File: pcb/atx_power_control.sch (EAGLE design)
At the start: 61 parts, among them IC2 REG1117, IC3 STM32F042F4, IC4 MY_7905DT, J1 ATX24RH, SW1 324_SW, SW2 324_SW, SW3 324_SW, SW4 324_SW, SW5 324_SW, SW7 324_SW, U1 USBC_16P, U2 USBC_16P

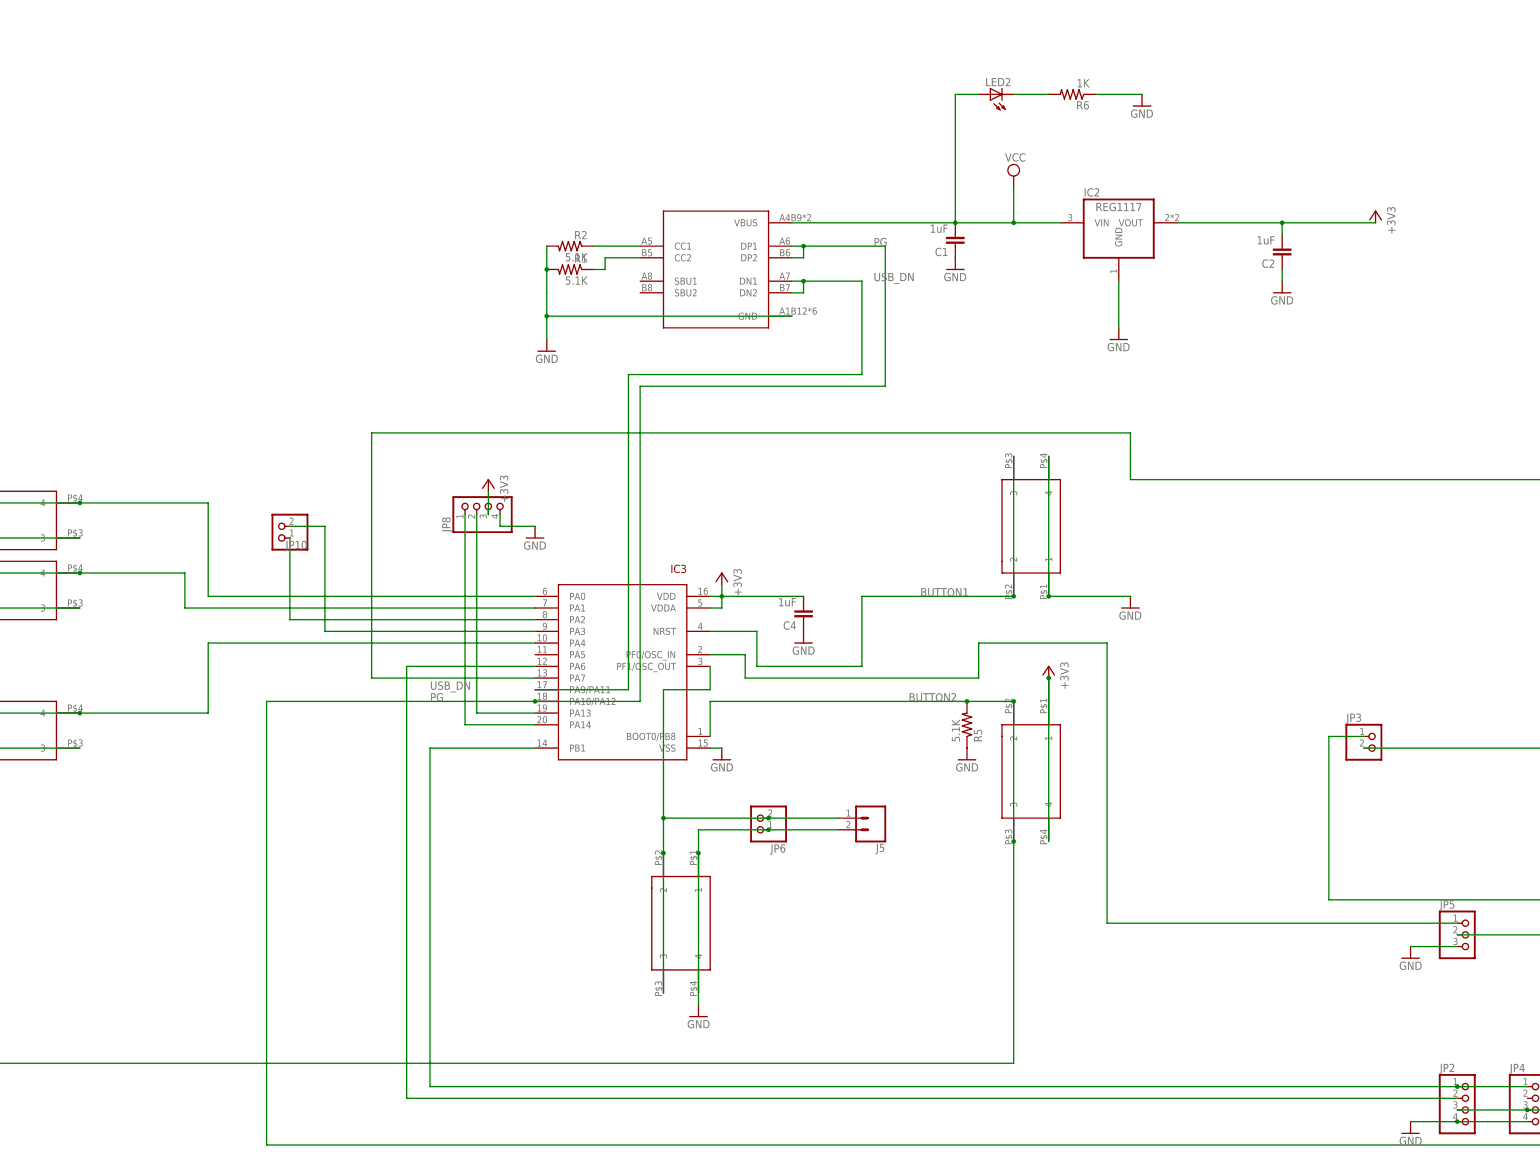
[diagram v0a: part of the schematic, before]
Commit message: added ds18b20 header
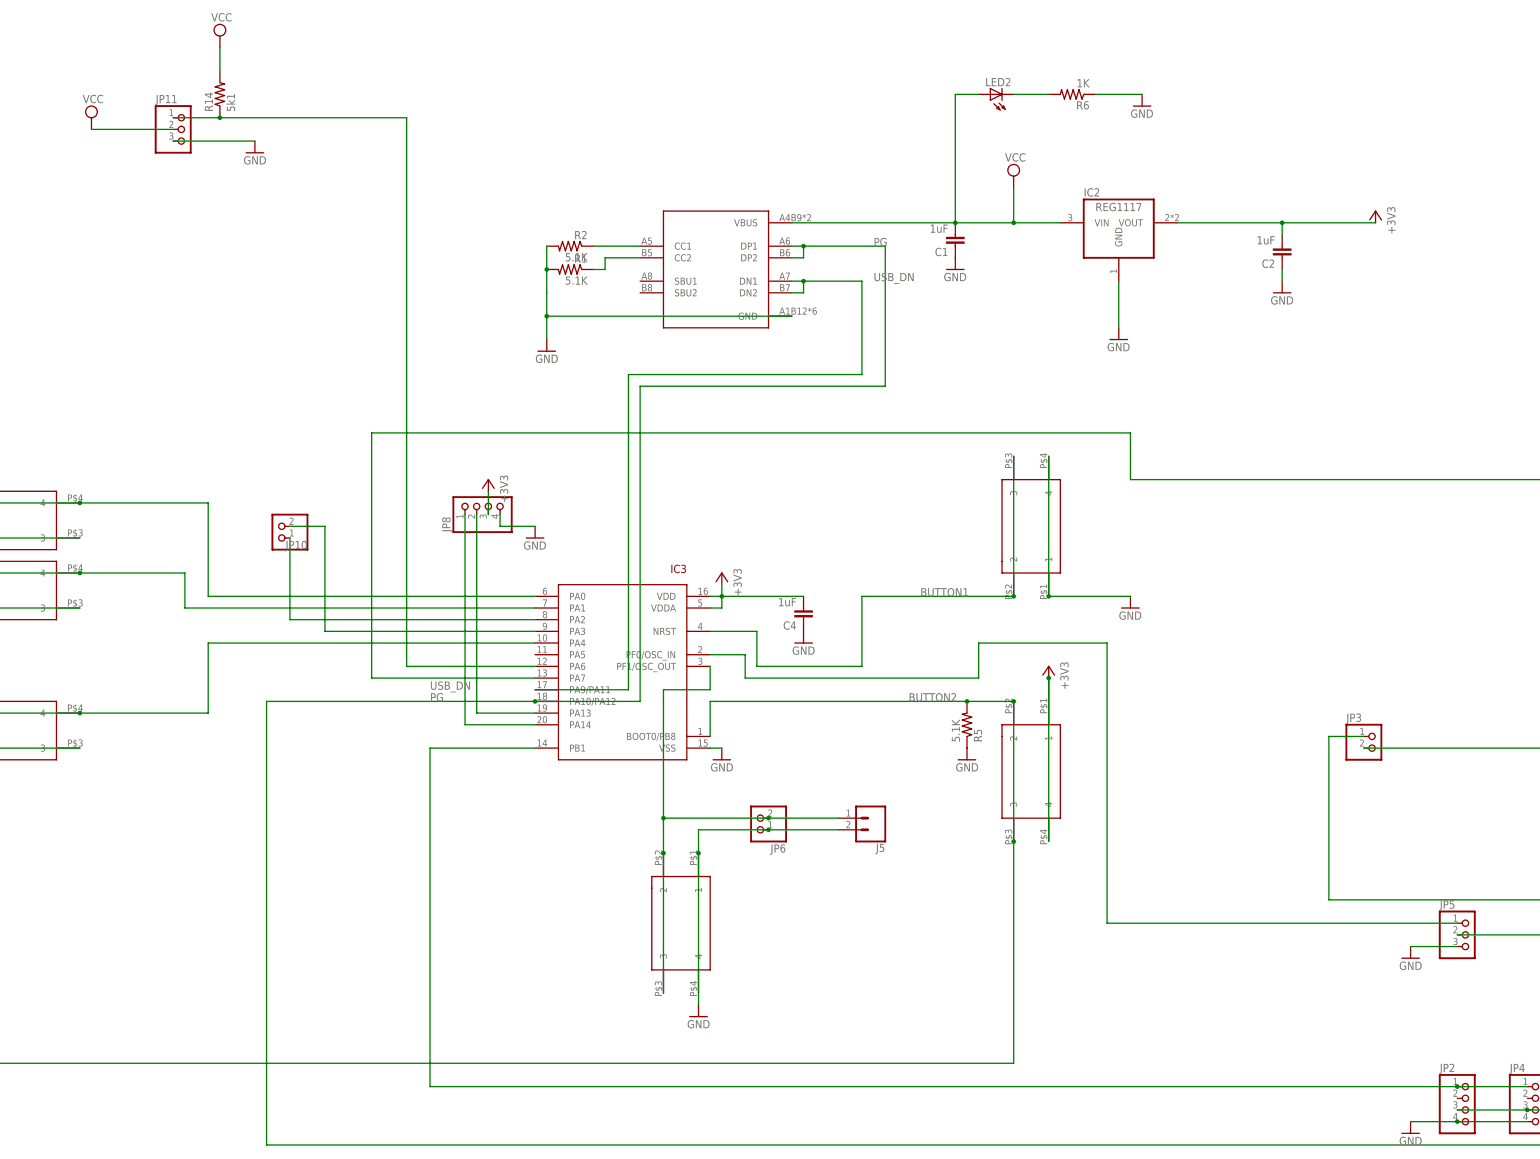
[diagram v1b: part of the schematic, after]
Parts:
- added JP11: (no value), adafruit_changed:PINHD-1X3CB
- added R14: 5k1, SparkFun-Passives:RESISTOR0805-RES
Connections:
- net GND: now also JP11.3
- net N$6: now also JP11.1, R14.1; no longer JP2.2
- net VCC: now also JP11.2, R14.2
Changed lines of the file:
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@@
 <part name="JP4" library="pinhead" library_urn="urn:adsk.eagle:library:325" deviceset="PINHD-1X4" device="" package3d_urn="urn:adsk.eagle:package:22407/2"/>
 <part name="JP12" library="adafruit_changed" deviceset="PINHD-1X6" device=""/>
+<part name="R14" library="SparkFun-Passives" deviceset="RESISTOR" device="0805-RES" value="5k1"/>
+<part name="JP11" library="adafruit_changed" deviceset="PINHD-1X3" device="CB"/>
+<part name="SUPPLY1" library="supply2" library_urn="urn:adsk.eagle:library:372" deviceset="VCC" device=""/>
+<part name="GND34" library="supply1" deviceset="GND" device=""/>
+<part name="SUPPLY2" library="supply2" library_urn="urn:adsk.eagle:library:372" deviceset="VCC" device=""/>
 </parts>
 <sheets>
@@
 <attribute name="NAME" x="273.05" y="71.755" size="1.778" layer="95"/>
 <attribute name="VALUE" x="273.05" y="50.8" size="1.778" layer="96"/>
+</instance>
+<instance part="R14" gate="G$1" x="-86.36" y="149.86" smashed="yes" rot="R90">
+<attribute name="NAME" x="-87.8586" y="146.05" size="1.778" layer="95" rot="R90"/>
+<attribute name="VALUE" x="-83.058" y="146.05" size="1.778" layer="96" rot="R90"/>
+</instance>
+<instance part="JP11" gate="A" x="-93.98" y="142.24" smashed="yes">
+<attribute name="NAME" x="-100.33" y="147.955" size="1.778" layer="95"/>
+<attribute name="VALUE" x="-100.33" y="134.62" size="1.778" layer="96"/>
+</instance>
+<instance part="SUPPLY1" gate="G$1" x="-114.3" y="144.78" smashed="yes">
+<attribute name="VALUE" x="-116.205" y="147.955" size="1.778" layer="96"/>
+</instance>
+<instance part="GND34" gate="1" x="-78.74" y="137.16" smashed="yes" rot="MR0">
+<attribute name="VALUE" x="-76.2" y="134.62" size="1.778" layer="96" rot="MR0"/>
+</instance>
+<instance part="SUPPLY2" gate="G$1" x="-86.36" y="162.56" smashed="yes">
+<attribute name="VALUE" x="-88.265" y="165.735" size="1.778" layer="96"/>
 </instance>
 </instances>
@@
 <junction x="317.5" y="76.2"/>
 </segment>
+<segment>
+<pinref part="GND34" gate="1" pin="GND"/>
+<pinref part="JP11" gate="A" pin="3"/>
+<wire x1="-78.74" y1="139.7" x2="-96.52" y2="139.7" width="0.1524" layer="91"/>
+</segment>
 </net>
 <net name="+3V3" class="0">
@@
 <wire x1="208.28" y1="7.62" x2="205.74" y2="7.62" width="0.1524" layer="91"/>
 <wire x1="205.74" y1="7.62" x2="162.56" y2="7.62" width="0.1524" layer="91"/>
+</segment>
+<segment>
+<pinref part="JP11" gate="A" pin="2"/>
+<pinref part="SUPPLY1" gate="G$1" pin="VCC"/>
+<wire x1="-96.52" y1="142.24" x2="-114.3" y2="142.24" width="0.1524" layer="91"/>
+</segment>
+<segment>
+<pinref part="R14" gate="G$1" pin="2"/>
+<pinref part="SUPPLY2" gate="G$1" pin="VCC"/>
+<wire x1="-86.36" y1="160.02" x2="-86.36" y2="154.94" width="0.1524" layer="91"/>
 </segment>
 </net>
@@
 <net name="N$6" class="0">
 <segment>
-<pinref part="JP2" gate="A" pin="2"/>
-<wire x1="182.88" y1="-68.58" x2="-45.72" y2="-68.58" width="0.1524" layer="91"/>
-<wire x1="-45.72" y1="-68.58" x2="-45.72" y2="25.4" width="0.1524" layer="91"/>
 <pinref part="IC3" gate="G$1" pin="PA6"/>
 <wire x1="-45.72" y1="25.4" x2="-17.78" y2="25.4" width="0.1524" layer="91"/>
-</segment>
-</net>
+<pinref part="JP11" gate="A" pin="1"/>
+<wire x1="-45.72" y1="25.4" x2="-45.72" y2="144.78" width="0.1524" layer="91"/>
+<wire x1="-45.72" y1="144.78" x2="-86.36" y2="144.78" width="0.1524" layer="91"/>
+<pinref part="R14" gate="G$1" pin="1"/>
+<wire x1="-86.36" y1="144.78" x2="-96.52" y2="144.78" width="0.1524" layer="91"/>
+<junction x="-86.36" y="144.78"/>
+</segment>
+</net>

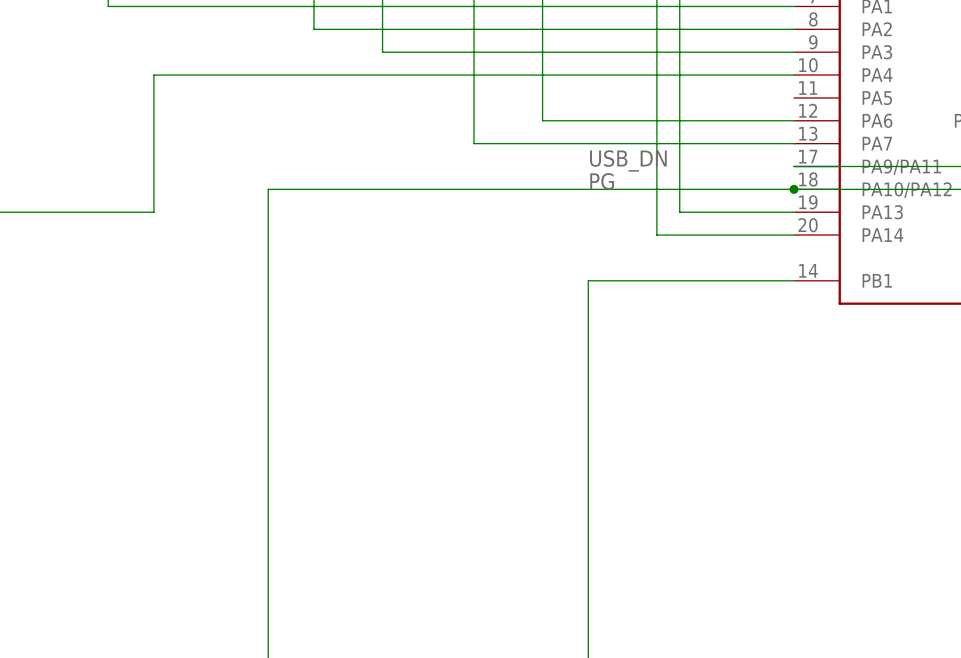
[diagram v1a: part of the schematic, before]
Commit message: added indicator LED
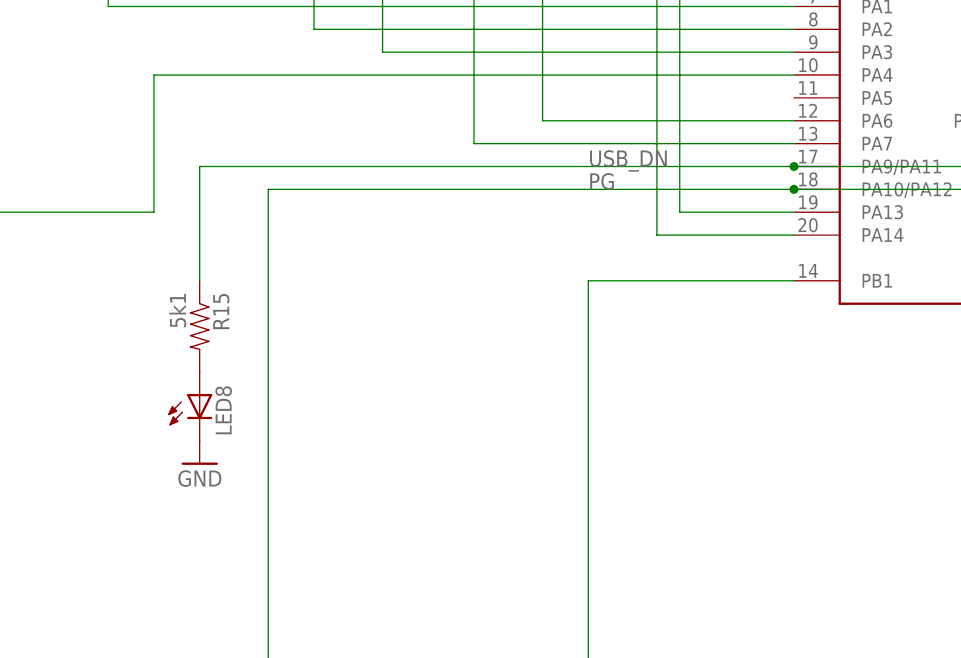
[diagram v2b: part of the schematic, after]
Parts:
- added LED8: (no value), adafruit:LEDCHIP-LED0805
- added R15: 5k1, SparkFun-Passives:RESISTOR0805-RES
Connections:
- new net N$19: LED8.A, R15.2
- net GND: now also LED8.C
- net USB_DN: now also R15.1
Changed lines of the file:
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@@
 <part name="GND34" library="supply1" deviceset="GND" device=""/>
 <part name="SUPPLY2" library="supply2" library_urn="urn:adsk.eagle:library:372" deviceset="VCC" device=""/>
+<part name="R15" library="SparkFun-Passives" deviceset="RESISTOR" device="0805-RES" value="5k1"/>
+<part name="LED8" library="adafruit" deviceset="LED" device="CHIP-LED0805"/>
+<part name="GND36" library="supply1" deviceset="GND" device=""/>
 </parts>
 <sheets>
@@
 <instance part="SUPPLY2" gate="G$1" x="-86.36" y="162.56" smashed="yes">
 <attribute name="VALUE" x="-88.265" y="165.735" size="1.778" layer="96"/>
+</instance>
+<instance part="R15" gate="G$1" x="-83.82" y="2.54" smashed="yes" rot="R270">
+<attribute name="NAME" x="-82.3214" y="6.35" size="1.778" layer="95" rot="R270"/>
+<attribute name="VALUE" x="-87.122" y="6.35" size="1.778" layer="96" rot="R270"/>
+</instance>
+<instance part="LED8" gate="G$1" x="-83.82" y="-5.08" smashed="yes">
+<attribute name="NAME" x="-80.264" y="-9.652" size="1.778" layer="95" rot="R90"/>
+<attribute name="VALUE" x="-78.105" y="-9.652" size="1.778" layer="96" rot="R90"/>
+</instance>
+<instance part="GND36" gate="1" x="-83.82" y="-12.7" smashed="yes" rot="MR0">
+<attribute name="VALUE" x="-81.28" y="-15.24" size="1.778" layer="96" rot="MR0"/>
 </instance>
 </instances>
@@
 <wire x1="-78.74" y1="139.7" x2="-96.52" y2="139.7" width="0.1524" layer="91"/>
 </segment>
+<segment>
+<pinref part="LED8" gate="G$1" pin="C"/>
+<pinref part="GND36" gate="1" pin="GND"/>
+</segment>
 </net>
 <net name="+3V3" class="0">
@@
 <wire x1="2.54" y1="88.9" x2="53.34" y2="88.9" width="0.1524" layer="91"/>
 <wire x1="53.34" y1="88.9" x2="53.34" y2="109.22" width="0.1524" layer="91"/>
+<pinref part="R15" gate="G$1" pin="1"/>
+<wire x1="-17.78" y1="20.32" x2="-83.82" y2="20.32" width="0.1524" layer="91"/>
+<wire x1="-83.82" y1="20.32" x2="-83.82" y2="7.62" width="0.1524" layer="91"/>
+<junction x="-17.78" y="20.32"/>
 </segment>
 </net>
@@
 </segment>
 </net>
+<net name="N$19" class="0">
+<segment>
+<pinref part="R15" gate="G$1" pin="2"/>
+<pinref part="LED8" gate="G$1" pin="A"/>
+</segment>
+</net>

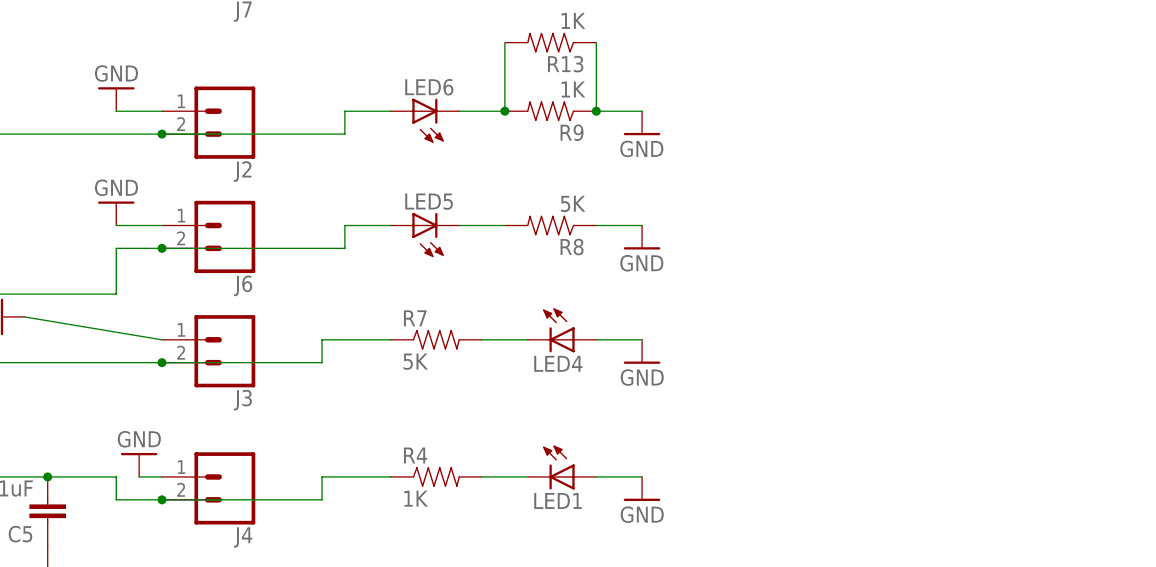
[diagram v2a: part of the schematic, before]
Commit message: adjusted LED resistor value, optimised GND plane
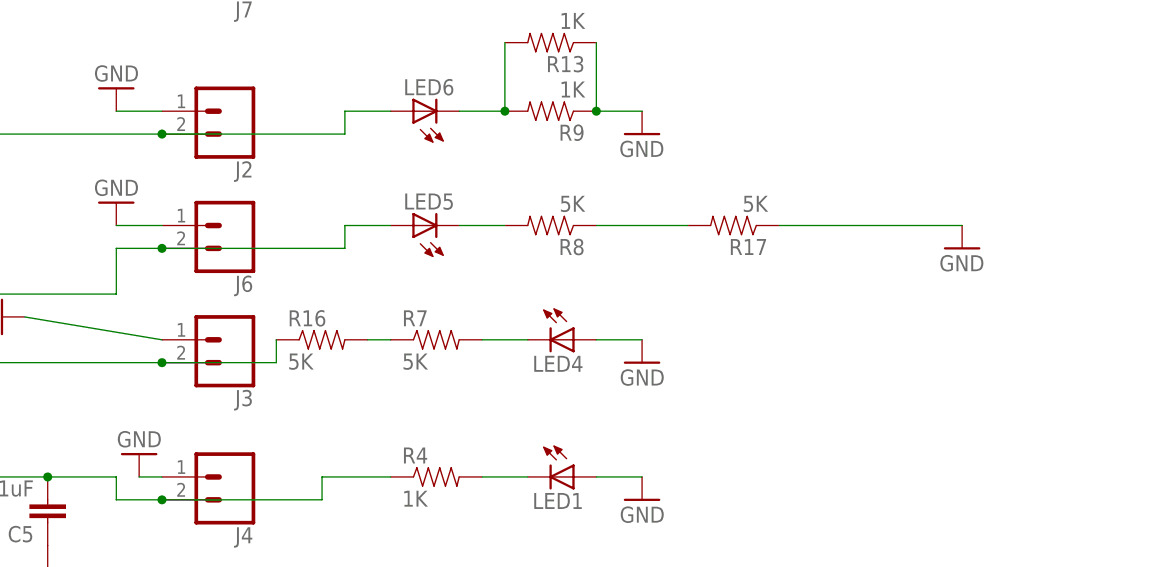
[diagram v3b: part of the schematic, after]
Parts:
- added R16, R17: 5K, SparkFun-Passives:RESISTOR0805-RES
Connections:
- new net N$28: R16.2, R7.1
- new net N$32: R17.2, R8.1
- net GND: now also R17.1; no longer R8.1
- net N$2: now also R16.1; no longer R7.1
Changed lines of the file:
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@@
 <part name="LED8" library="adafruit" deviceset="LED" device="CHIP-LED0805"/>
 <part name="GND36" library="supply1" deviceset="GND" device=""/>
+<part name="R16" library="SparkFun-Passives" deviceset="RESISTOR" device="0805-RES" value="5K"/>
+<part name="R17" library="SparkFun-Passives" deviceset="RESISTOR" device="0805-RES" value="5K"/>
 </parts>
 <sheets>
@@
 <attribute name="VALUE" x="394.97" y="16.002" size="1.778" layer="96" rot="R180"/>
 </instance>
-<instance part="GND19" gate="1" x="401.32" y="10.16" smashed="yes">
-<attribute name="VALUE" x="398.78" y="7.62" size="1.778" layer="96"/>
+<instance part="GND19" gate="1" x="436.88" y="10.16" smashed="yes">
+<attribute name="VALUE" x="434.34" y="7.62" size="1.778" layer="96"/>
 </instance>
 <instance part="LED6" gate="G$1" x="375.92" y="25.4" smashed="yes" rot="R90">
@@
 <instance part="GND36" gate="1" x="-83.82" y="-12.7" smashed="yes" rot="MR0">
 <attribute name="VALUE" x="-81.28" y="-15.24" size="1.778" layer="96" rot="MR0"/>
+</instance>
+<instance part="R16" gate="G$1" x="365.76" y="0" smashed="yes">
+<attribute name="NAME" x="361.95" y="1.4986" size="1.778" layer="95"/>
+<attribute name="VALUE" x="361.95" y="-3.302" size="1.778" layer="96"/>
+</instance>
+<instance part="R17" gate="G$1" x="411.48" y="12.7" smashed="yes" rot="R180">
+<attribute name="NAME" x="415.29" y="11.2014" size="1.778" layer="95" rot="R180"/>
+<attribute name="VALUE" x="415.29" y="16.002" size="1.778" layer="96" rot="R180"/>
 </instance>
 </instances>
@@
 </segment>
 <segment>
-<pinref part="R8" gate="G$1" pin="1"/>
 <pinref part="GND19" gate="1" pin="GND"/>
-<wire x1="401.32" y1="12.7" x2="396.24" y2="12.7" width="0.1524" layer="91"/>
+<wire x1="436.88" y1="12.7" x2="416.56" y2="12.7" width="0.1524" layer="91"/>
+<pinref part="R17" gate="G$1" pin="1"/>
 </segment>
 <segment>
@@
 <wire x1="248.92" y1="-2.54" x2="297.18" y2="-2.54" width="0.1524" layer="91"/>
 <junction x="297.18" y="-2.54"/>
-<pinref part="R7" gate="G$1" pin="1"/>
-<wire x1="365.76" y1="0" x2="373.38" y2="0" width="0.1524" layer="91"/>
 <pinref part="J3" gate="G$1" pin="2"/>
-<wire x1="347.98" y1="-2.54" x2="365.76" y2="-2.54" width="0.1524" layer="91"/>
-<wire x1="365.76" y1="-2.54" x2="365.76" y2="0" width="0.1524" layer="91"/>
+<wire x1="347.98" y1="-2.54" x2="360.68" y2="-2.54" width="0.1524" layer="91"/>
+<wire x1="360.68" y1="-2.54" x2="360.68" y2="0" width="0.1524" layer="91"/>
 <junction x="347.98" y="-2.54"/>
+<pinref part="R16" gate="G$1" pin="1"/>
 </segment>
 </net>
@@
 </segment>
 </net>
+<net name="N$28" class="0">
+<segment>
+<pinref part="R7" gate="G$1" pin="1"/>
+<wire x1="370.84" y1="0" x2="373.38" y2="0" width="0.1524" layer="91"/>
+<pinref part="R16" gate="G$1" pin="2"/>
+</segment>
+</net>
+<net name="N$32" class="0">
+<segment>
+<pinref part="R8" gate="G$1" pin="1"/>
+<wire x1="406.4" y1="12.7" x2="396.24" y2="12.7" width="0.1524" layer="91"/>
+<pinref part="R17" gate="G$1" pin="2"/>
+</segment>
+</net>
